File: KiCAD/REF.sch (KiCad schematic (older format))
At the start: 7 parts, among them J21 Conn_01x04, J22 Conn_01x04, U7 ADR4525

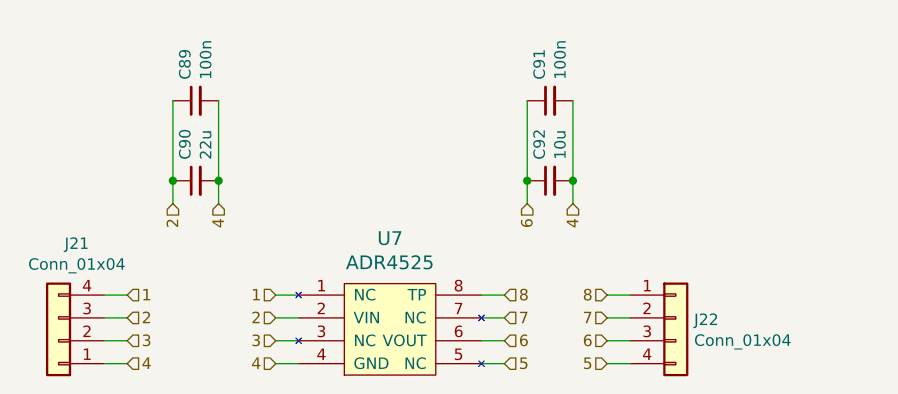
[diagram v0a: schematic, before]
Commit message: added usb, crystals
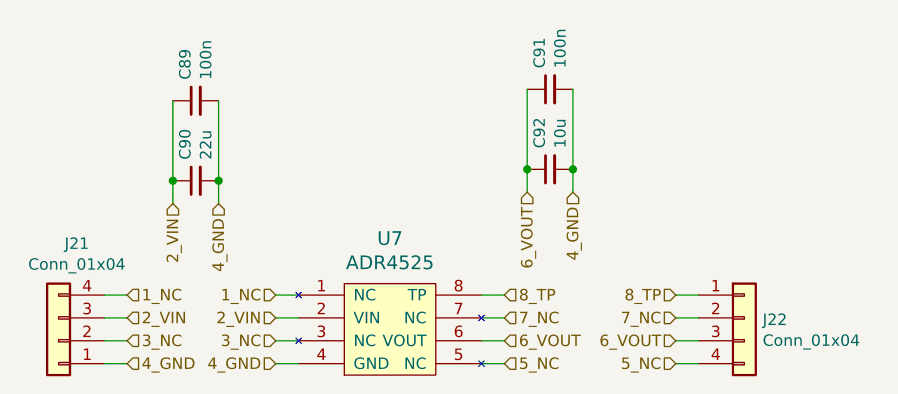
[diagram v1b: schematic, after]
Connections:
- net 1 renamed 1_NC
- net 2 renamed 2_VIN
- net 3 renamed 3_NC
- net 4 renamed 4_GND
- net 5 renamed 5_NC
- net 6 renamed 6_VOUT
- net 7 renamed 7_NC
- net 8 renamed 8_TP
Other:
- moved on the sheet: C91, C92, J22
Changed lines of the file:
@@
 $Descr A4 11693 8268
 encoding utf-8
-Sheet 8 17
+Sheet 8 18
 Title ""
 Date ""
@@
 L Connector_Generic:Conn_01x04 J?
 U 1 1 5CDACE19
-P 7200 3800
+P 7500 3800
 AR Path="/5CDACE19" Ref="J?"  Part="1"
 AR Path="/5CDACD1E/5CDACE19" Ref="J22"  Part="1"
-F 0 "J22" H 7280 3792 50  0000 L CNN
-F 1 "Conn_01x04" H 7280 3701 50  0000 L CNN
-F 2 "Connector_PinHeader_2.54mm:PinHeader_1x04_P2.54mm_Vertical" H 7200 3800 50  0001 C CNN
-F 3 "~" H 7200 3800 50  0001 C CNN
-	1    7200 3800
+F 0 "J22" H 7580 3792 50  0000 L CNN
+F 1 "Conn_01x04" H 7580 3701 50  0000 L CNN
+F 2 "Connector_PinHeader_2.54mm:PinHeader_1x04_P2.54mm_Vertical" H 7500 3800 50  0001 C CNN
+F 3 "~" H 7500 3800 50  0001 C CNN
+	1    7500 3800
 	1    0    0    -1
 $EndComp
@@
 $EndComp
 Text HLabel 5450 3800 0    50   Input ~ 0
-2
+2_VIN
 Wire Wire Line
 	5450 3800 5550 3800
 Text HLabel 5450 4000 0    50   Input ~ 0
-4
+4_GND
 Wire Wire Line
 	5450 4000 5550 4000
 Text HLabel 6450 3900 2    50   Input ~ 0
-6
+6_VOUT
 Text HLabel 6450 3700 2    50   Input ~ 0
-8
+8_TP
 Text HLabel 4800 3800 2    50   Input ~ 0
-2
+2_VIN
 Wire Wire Line
 	4800 3800 4700 3800
 Text HLabel 4800 4000 2    50   Input ~ 0
-4
+4_GND
 Wire Wire Line
 	4800 4000 4700 4000
@@
 Wire Wire Line
 	6450 3900 6350 3900
-Text HLabel 6900 3900 0    50   Input ~ 0
-6
-Text HLabel 6900 3700 0    50   Input ~ 0
-8
-Wire Wire Line
-	6900 3700 7000 3700
-Wire Wire Line
-	6900 3900 7000 3900
-Text HLabel 6550 3300 3    50   Input ~ 0
-6
-Text HLabel 6750 3300 3    50   Input ~ 0
-4
+Text HLabel 7200 3900 0    50   Input ~ 0
+6_VOUT
+Text HLabel 7200 3700 0    50   Input ~ 0
+8_TP
+Wire Wire Line
+	7200 3700 7300 3700
+Wire Wire Line
+	7200 3900 7300 3900
+Text HLabel 6550 3250 3    50   Input ~ 0
+6_VOUT
+Text HLabel 6750 3250 3    50   Input ~ 0
+4_GND
 $Comp
 L Device:C_Small C?
 U 1 1 5CDACE39
-P 6650 2850
+P 6650 2800
 AR Path="/5CDBF57D/5CDACE39" Ref="C?"  Part="1"
 AR Path="/5CE92451/5CDACE39" Ref="C?"  Part="1"
@@
 AR Path="/5CDACE39" Ref="C?"  Part="1"
 AR Path="/5CDACD1E/5CDACE39" Ref="C91"  Part="1"
-F 0 "C91" H 6742 2896 50  0000 L CNN
-F 1 "100n" H 6742 2805 50  0000 L CNN
-F 2 "Capacitor_SMD:C_0402_1005Metric" H 6650 2850 50  0001 C CNN
-F 3 "~" H 6650 2850 50  0001 C CNN
-	1    6650 2850
+F 0 "C91" H 6742 2846 50  0000 L CNN
+F 1 "100n" H 6742 2755 50  0000 L CNN
+F 2 "Capacitor_SMD:C_0402_1005Metric" H 6650 2800 50  0001 C CNN
+F 3 "~" H 6650 2800 50  0001 C CNN
+	1    6650 2800
 	0    -1   -1   0
 $EndComp
@@
 L Device:C_Small C?
 U 1 1 5CDACE40
-P 6650 3200
+P 6650 3150
 AR Path="/5CDBF57D/5CDACE40" Ref="C?"  Part="1"
 AR Path="/5CE92451/5CDACE40" Ref="C?"  Part="1"
@@
 AR Path="/5CDACE40" Ref="C?"  Part="1"
 AR Path="/5CDACD1E/5CDACE40" Ref="C92"  Part="1"
-F 0 "C92" H 6742 3246 50  0000 L CNN
-F 1 "10u" H 6742 3155 50  0000 L CNN
-F 2 "Capacitor_SMD:C_0603_1608Metric" H 6650 3200 50  0001 C CNN
-F 3 "~" H 6650 3200 50  0001 C CNN
-	1    6650 3200
-	0    -1   -1   0
-$EndComp
-Wire Wire Line
-	6550 3300 6550 3200
-Wire Wire Line
-	6750 3300 6750 3200
-Wire Wire Line
-	6550 3200 6550 2850
-Connection ~ 6550 3200
-Wire Wire Line
-	6750 3200 6750 2850
-Connection ~ 6750 3200
+F 0 "C92" H 6742 3196 50  0000 L CNN
+F 1 "10u" H 6742 3105 50  0000 L CNN
+F 2 "Capacitor_SMD:C_0603_1608Metric" H 6650 3150 50  0001 C CNN
+F 3 "~" H 6650 3150 50  0001 C CNN
+	1    6650 3150
+	0    -1   -1   0
+$EndComp
+Wire Wire Line
+	6550 3250 6550 3150
+Wire Wire Line
+	6750 3250 6750 3150
+Wire Wire Line
+	6550 3150 6550 2800
+Connection ~ 6550 3150
+Wire Wire Line
+	6750 3150 6750 2800
+Connection ~ 6750 3150
 Text HLabel 5000 3300 3    50   Input ~ 0
-2
+2_VIN
 Text HLabel 5200 3300 3    50   Input ~ 0
-4
+4_GND
 $Comp
 L Device:C_Small C?
@@
 Connection ~ 5200 3200
 Text HLabel 5450 3700 0    50   Input ~ 0
-1
+1_NC
 Wire Wire Line
 	5450 3700 5550 3700
 Text HLabel 5450 3900 0    50   Input ~ 0
-3
+3_NC
 Wire Wire Line
 	5450 3900 5550 3900
 Text HLabel 4800 3700 2    50   Input ~ 0
-1
+1_NC
 Wire Wire Line
 	4800 3700 4700 3700
 Text HLabel 4800 3900 2    50   Input ~ 0
-3
+3_NC
 Wire Wire Line
 	4800 3900 4700 3900
 Text HLabel 6450 4000 2    50   Input ~ 0
-5
+5_NC
 Text HLabel 6450 3800 2    50   Input ~ 0
-7
+7_NC
 Wire Wire Line
 	6450 3800 6350 3800
 Wire Wire Line
 	6450 4000 6350 4000
-Text HLabel 6900 4000 0    50   Input ~ 0
-5
-Text HLabel 6900 3800 0    50   Input ~ 0
-7
-Wire Wire Line
-	6900 3800 7000 3800
-Wire Wire Line
-	6900 4000 7000 4000
+Text HLabel 7200 4000 0    50   Input ~ 0
+5_NC
+Text HLabel 7200 3800 0    50   Input ~ 0
+7_NC
+Wire Wire Line
+	7200 3800 7300 3800
+Wire Wire Line
+	7200 4000 7300 4000
 $EndSCHEMATC
